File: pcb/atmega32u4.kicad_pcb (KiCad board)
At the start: 2 copper layers, 15 parts, among them CON1 ISP, P1 CONN_01X14, P2 CONN_01X14, P3 USB_OTG, U1 ATmega32U4-AU, Y1 16MHz

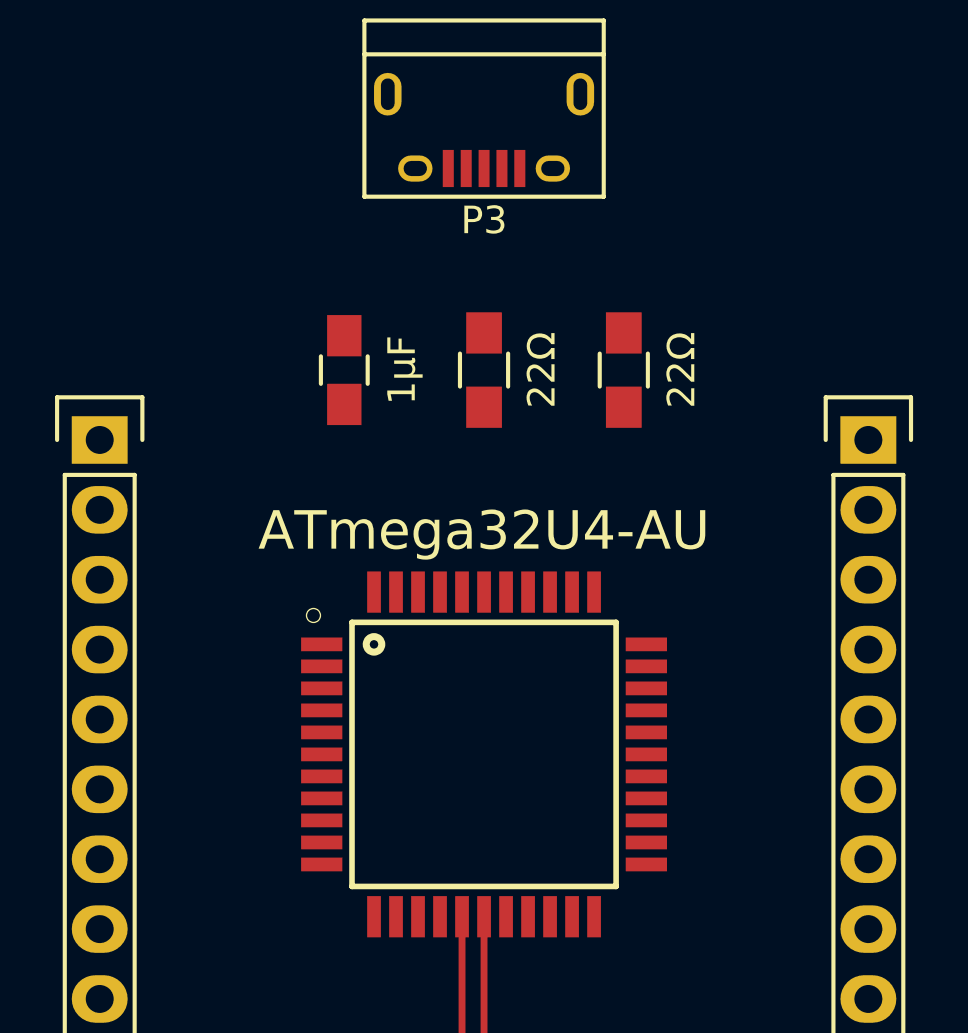
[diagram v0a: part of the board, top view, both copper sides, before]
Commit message: Hook up most of the left side
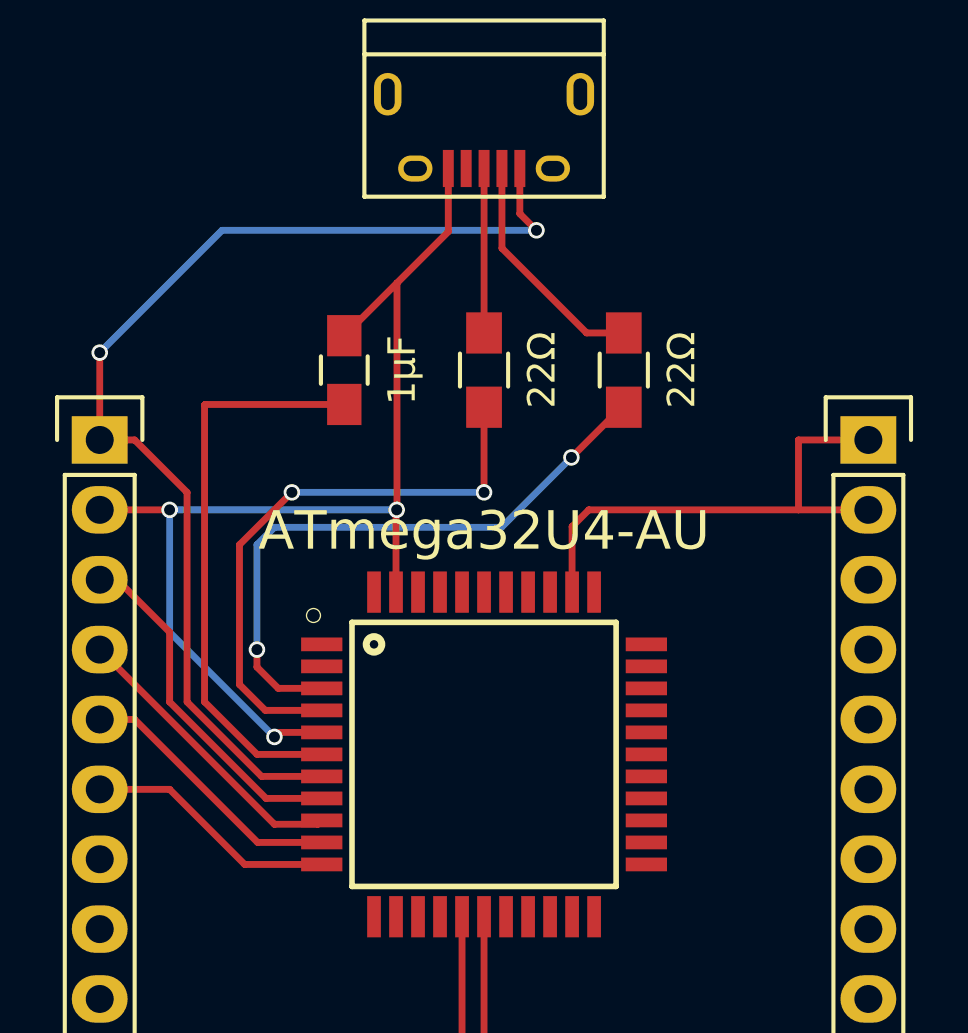
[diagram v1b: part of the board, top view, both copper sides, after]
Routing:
- net GND: track 14.8 -> 74.6 mm, vias 0 -> 3
- net /VCC: track 0.00 -> 41.0 mm, vias 0 -> 2
- net Net-(R2-Pad1): track 0.00 -> 22.5 mm, vias 0 -> 2
- net Net-(R1-Pad1): track 0.00 -> 21.2 mm, vias 0 -> 2
- net Net-(C4-Pad1): track 0.00 -> 20.9 mm
- net /PB0: track 0.00 -> 12.9 mm
- net /ISP_SCK/PB1: track 0.00 -> 10.8 mm
- net /ISP_MOSI/PB2: track 0.00 -> 9.92 mm
- net /ISP_MISO/PB3: track 0.00 -> 9.20 mm
- net Net-(P3-Pad2): track 0.00 -> 8.60 mm
- net Net-(P3-Pad3): track 0.00 -> 5.98 mm
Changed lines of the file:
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@@
   (general
     (links 67)
-    (no_connects 59)
-    (area 119.426667 76.267 157.433334 145.733809)
+    (no_connects 42)
+    (area 119.426667 76.775 157.433334 145.733809)
     (thickness 1.6)
     (drawings 0)
-    (tracks 26)
+    (tracks 103)
     (zones 0)
     (modules 15)
@@
     (38 B.Mask user)
     (39 F.Mask user)
-    (40 Dwgs.User user)
+    (40 Dwgs.User user hide)
     (41 Cmts.User user)
     (42 Eco1.User user)
@@
     (tags "USB USB_B USB_micro USB_OTG")
     (attr smd)
-    (fp_text reference P3 (at 0 -3.45 180) (layer F.SilkS)
+    (fp_text reference P3 (at 0 -3.45 180) (layer F.SilkS) hide
       (effects (font (size 1 1) (thickness 0.15)))
     )
@@
   (segment (start 135.89 135.89) (end 135.89 133.35) (width 0.25) (layer F.Cu) (net 1))
   (segment (start 135.89 133.35) (end 137.18 133.35) (width 0.25) (layer F.Cu) (net 1))
+  (segment (start 127 100.965) (end 127 96.52) (width 0.25) (layer B.Cu) (net 2))
+  (segment (start 130.81 104.775) (end 127 100.965) (width 0.25) (layer B.Cu) (net 2))
+  (via (at 130.81 104.775) (size 0.6) (drill 0.4) (layers F.Cu B.Cu) (net 2))
+  (segment (start 130.975 104.61) (end 130.81 104.775) (width 0.25) (layer F.Cu) (net 2))
+  (segment (start 132.53 104.61) (end 130.975 104.61) (width 0.25) (layer F.Cu) (net 2))
+  (segment (start 135.265 88.275) (end 135.265 96.51) (width 0.25) (layer F.Cu) (net 2))
+  (segment (start 135.265 96.51) (end 135.255 96.52) (width 0.25) (layer F.Cu) (net 2))
+  (segment (start 124.46 96.52) (end 127 96.52) (width 0.25) (layer F.Cu) (net 2))
+  (via (at 127 96.52) (size 0.6) (drill 0.4) (layers F.Cu B.Cu) (net 2))
+  (segment (start 127 96.52) (end 135.255 96.52) (width 0.25) (layer B.Cu) (net 2))
+  (via (at 135.255 96.52) (size 0.6) (drill 0.4) (layers F.Cu B.Cu) (net 2))
+  (segment (start 135.23 96.545) (end 135.23 99.51) (width 0.25) (layer F.Cu) (net 2))
+  (segment (start 135.255 96.52) (end 135.23 96.545) (width 0.25) (layer F.Cu) (net 2))
+  (segment (start 149.86 96.52) (end 149.86 93.98) (width 0.25) (layer F.Cu) (net 2))
+  (segment (start 149.86 93.98) (end 152.4 93.98) (width 0.25) (layer F.Cu) (net 2))
+  (segment (start 141.63 99.51) (end 141.63 97.13) (width 0.25) (layer F.Cu) (net 2))
+  (segment (start 142.24 96.52) (end 149.86 96.52) (width 0.25) (layer F.Cu) (net 2))
+  (segment (start 149.86 96.52) (end 152.4 96.52) (width 0.25) (layer F.Cu) (net 2))
+  (segment (start 141.63 97.13) (end 142.24 96.52) (width 0.25) (layer F.Cu) (net 2))
+  (segment (start 137.1309 84.11254) (end 137.1309 86.4091) (width 0.25) (layer F.Cu) (net 2))
+  (segment (start 137.1309 86.4091) (end 135.265 88.275) (width 0.25) (layer F.Cu) (net 2))
+  (segment (start 135.265 88.275) (end 133.35 90.19) (width 0.25) (layer F.Cu) (net 2))
   (segment (start 139.68 135.91) (end 139.68 133.35) (width 0.25) (layer F.Cu) (net 2))
   (segment (start 138.43 137.16) (end 139.68 135.91) (width 0.25) (layer F.Cu) (net 2))
@@
   (segment (start 143.49 132.08) (end 143.51 132.1) (width 0.25) (layer F.Cu) (net 2))
   (segment (start 139.68 133.35) (end 139.7 133.35) (width 0.25) (layer F.Cu) (net 2))
+  (segment (start 132.53 105.41) (end 130.179194 105.41) (width 0.25) (layer F.Cu) (net 3))
+  (segment (start 128.29 92.69) (end 133.35 92.69) (width 0.25) (layer F.Cu) (net 3))
+  (segment (start 128.27 92.71) (end 128.29 92.69) (width 0.25) (layer F.Cu) (net 3))
+  (segment (start 128.27 103.500806) (end 128.27 92.71) (width 0.25) (layer F.Cu) (net 3))
+  (segment (start 130.179194 105.41) (end 128.27 103.500806) (width 0.25) (layer F.Cu) (net 3))
   (segment (start 140.97 124.48) (end 140.97 118.71706) (width 0.25) (layer F.Cu) (net 4))
   (segment (start 140.97 118.71706) (end 140.87094 118.618) (width 0.25) (layer F.Cu) (net 4))
@@
   (segment (start 137.63 111.31) (end 137.63 116.97706) (width 0.25) (layer F.Cu) (net 5))
   (segment (start 137.63 116.97706) (end 135.98906 118.618) (width 0.25) (layer F.Cu) (net 5))
+  (segment (start 124.46 99.06) (end 125.095 99.06) (width 0.25) (layer F.Cu) (net 7))
+  (segment (start 125.095 99.06) (end 127 100.965) (width 0.25) (layer F.Cu) (net 7))
+  (segment (start 127 100.965) (end 127 103.503602) (width 0.25) (layer F.Cu) (net 7))
+  (segment (start 127 103.503602) (end 130.506398 107.01) (width 0.25) (layer F.Cu) (net 7))
+  (segment (start 130.506398 107.01) (end 132.53 107.01) (width 0.25) (layer F.Cu) (net 7))
+  (segment (start 124.46 101.6) (end 130.81 107.95) (width 0.25) (layer F.Cu) (net 8))
+  (segment (start 130.81 107.95) (end 132.39 107.95) (width 0.25) (layer F.Cu) (net 8))
+  (segment (start 132.39 107.95) (end 132.53 107.81) (width 0.25) (layer F.Cu) (net 8))
+  (segment (start 124.46 104.14) (end 125.73 104.14) (width 0.25) (layer F.Cu) (net 9))
+  (segment (start 130.2 108.61) (end 132.53 108.61) (width 0.25) (layer F.Cu) (net 9))
+  (segment (start 125.73 104.14) (end 130.2 108.61) (width 0.25) (layer F.Cu) (net 9))
+  (segment (start 124.46 106.68) (end 127 106.68) (width 0.25) (layer F.Cu) (net 10))
+  (segment (start 129.73 109.41) (end 132.53 109.41) (width 0.25) (layer F.Cu) (net 10))
+  (segment (start 127 106.68) (end 129.73 109.41) (width 0.25) (layer F.Cu) (net 10))
+  (segment (start 142.16 90.09) (end 143.51 90.09) (width 0.25) (layer F.Cu) (net 31))
+  (segment (start 139.0809 87.0109) (end 142.16 90.09) (width 0.25) (layer F.Cu) (net 31))
+  (segment (start 139.0809 84.11254) (end 139.0809 87.0109) (width 0.25) (layer F.Cu) (net 31))
+  (segment (start 138.4309 84.11254) (end 138.4309 90.0891) (width 0.25) (layer F.Cu) (net 32))
+  (segment (start 138.4309 90.0891) (end 138.43 90.09) (width 0.25) (layer F.Cu) (net 32))
+  (segment (start 138.43 95.885) (end 138.43 92.79) (width 0.25) (layer F.Cu) (net 35))
+  (via (at 138.43 95.885) (size 0.6) (drill 0.4) (layers F.Cu B.Cu) (net 35))
+  (segment (start 131.445 95.885) (end 138.43 95.885) (width 0.25) (layer B.Cu) (net 35))
+  (via (at 131.445 95.885) (size 0.6) (drill 0.4) (layers F.Cu B.Cu) (net 35))
+  (segment (start 129.54 97.79) (end 131.445 95.885) (width 0.25) (layer F.Cu) (net 35))
+  (segment (start 129.54 102.87) (end 129.54 97.79) (width 0.25) (layer F.Cu) (net 35))
+  (segment (start 130.48 103.81) (end 129.54 102.87) (width 0.25) (layer F.Cu) (net 35))
+  (segment (start 132.53 103.81) (end 130.48 103.81) (width 0.25) (layer F.Cu) (net 35))
+  (segment (start 132.53 103.01) (end 130.95 103.01) (width 0.25) (layer F.Cu) (net 36))
+  (segment (start 141.605 94.615) (end 143.43 92.79) (width 0.25) (layer F.Cu) (net 36))
+  (via (at 141.605 94.615) (size 0.6) (drill 0.4) (layers F.Cu B.Cu) (net 36))
+  (segment (start 139.065 97.155) (end 141.605 94.615) (width 0.25) (layer B.Cu) (net 36))
+  (segment (start 130.81 97.155) (end 139.065 97.155) (width 0.25) (layer B.Cu) (net 36))
+  (segment (start 130.175 97.79) (end 130.81 97.155) (width 0.25) (layer B.Cu) (net 36))
+  (segment (start 130.175 101.6) (end 130.175 97.79) (width 0.25) (layer B.Cu) (net 36))
+  (via (at 130.175 101.6) (size 0.6) (drill 0.4) (layers F.Cu B.Cu) (net 36))
+  (segment (start 130.175 102.235) (end 130.175 101.6) (width 0.25) (layer F.Cu) (net 36))
+  (segment (start 130.95 103.01) (end 130.175 102.235) (width 0.25) (layer F.Cu) (net 36))
+  (segment (start 143.43 92.79) (end 143.51 92.79) (width 0.25) (layer F.Cu) (net 36))
+  (segment (start 132.53 106.21) (end 130.342796 106.21) (width 0.25) (layer F.Cu) (net 40))
+  (segment (start 125.73 93.98) (end 124.46 93.98) (width 0.25) (layer F.Cu) (net 40))
+  (segment (start 127.635 95.885) (end 125.73 93.98) (width 0.25) (layer F.Cu) (net 40))
+  (segment (start 127.635 103.502204) (end 127.635 95.885) (width 0.25) (layer F.Cu) (net 40))
+  (segment (start 130.342796 106.21) (end 127.635 103.502204) (width 0.25) (layer F.Cu) (net 40))
+  (segment (start 140.335 86.36) (end 128.905 86.36) (width 0.25) (layer B.Cu) (net 40))
+  (segment (start 139.7309 84.11254) (end 139.7309 85.7559) (width 0.25) (layer F.Cu) (net 40))
+  (via (at 140.335 86.36) (size 0.6) (drill 0.4) (layers F.Cu B.Cu) (net 40))
+  (segment (start 139.7309 85.7559) (end 140.335 86.36) (width 0.25) (layer F.Cu) (net 40))
+  (segment (start 124.46 90.805) (end 124.46 93.98) (width 0.25) (layer F.Cu) (net 40))
+  (via (at 124.46 90.805) (size 0.6) (drill 0.4) (layers F.Cu B.Cu) (net 40))
+  (segment (start 128.905 86.36) (end 124.46 90.805) (width 0.25) (layer B.Cu) (net 40))
 )
